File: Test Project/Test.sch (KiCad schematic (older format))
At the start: 1 part

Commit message: Summer
Added very important component layout
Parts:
- added L? (x2): 20, symbol INDUCTOR
- added R? (x2): 120, symbol R
- added U?: MCP2551-I/SN, SO-8, symbol MCP2551-I/SN
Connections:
- net at U?.6 (CANL): now also R?.2
- net at U?.7 (CANH): now also L?.2
- new net: L?.1, R?.1
- new net: L?.2, U?.7 (CANH)
- new net: R?.1, U?.6 (CANL)
- new net: L?.1, R?.2
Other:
- moved on the sheet: U?
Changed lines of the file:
@@
 LIBS:memory
 LIBS:xilinx
-LIBS:special
 LIBS:microcontrollers
 LIBS:dsp
@@
 L MCP2551-I/SN U?
 U 1 1 559C6BBA
-P 4800 3800
-F 0 "U?" H 4400 4150 50  0000 L CNN
-F 1 "MCP2551-I/SN" H 4900 4150 50  0000 L CNN
-F 2 "SO-8" H 4800 3800 50  0000 C CIN
-F 3 "" H 4800 3800 60  0000 C CNN
-	1    4800 3800
+P 4600 3600
+F 0 "U?" H 4200 3950 50  0000 L CNN
+F 1 "MCP2551-I/SN" H 4700 3950 50  0000 L CNN
+F 2 "SO-8" H 4600 3600 50  0000 C CIN
+F 3 "" H 4600 3600 60  0000 C CNN
+	1    4600 3600
 	1    0    0    -1
 $EndComp
+$Comp
+L INDUCTOR L?
+U 1 1 559DCECC
+P 6100 2400
+F 0 "L?" V 6050 2400 50  0000 C CNN
+F 1 "20" V 6200 2400 50  0000 C CNN
+F 2 "" H 6100 2400 60  0000 C CNN
+F 3 "" H 6100 2400 60  0000 C CNN
+	1    6100 2400
+	1    0    0    -1
+$EndComp
+$Comp
+L MCP2551-I/SN U?
+U 1 1 559DD087
+P 6850 3600
+F 0 "U?" H 6450 3950 50  0000 L CNN
+F 1 "MCP2551-I/SN" H 6950 3950 50  0000 L CNN
+F 2 "SO-8" H 6850 3600 50  0000 C CIN
+F 3 "" H 6850 3600 60  0000 C CNN
+	1    6850 3600
+	-1   0    0    -1
+$EndComp
+$Comp
+L INDUCTOR L?
+U 1 1 559DD128
+P 5400 2400
+F 0 "L?" V 5350 2400 50  0000 C CNN
+F 1 "20" V 5500 2400 50  0000 C CNN
+F 2 "" H 5400 2400 60  0000 C CNN
+F 3 "" H 5400 2400 60  0000 C CNN
+	1    5400 2400
+	-1   0    0    -1
+$EndComp
+Wire Wire Line
+	5400 2700 5400 3500
+Wire Wire Line
+	5400 3500 5100 3500
+$Comp
+L R R?
+U 1 1 559DD2E2
+P 5750 1600
+F 0 "R?" V 5830 1600 50  0000 C CNN
+F 1 "120" V 5750 1600 50  0000 C CNN
+F 2 "" V 5680 1600 30  0000 C CNN
+F 3 "" H 5750 1600 30  0000 C CNN
+	1    5750 1600
+	0    1    1    0
+$EndComp
+$Comp
+L R R?
+U 1 1 559DD3B4
+P 5750 3700
+F 0 "R?" V 5830 3700 50  0000 C CNN
+F 1 "120" V 5750 3700 50  0000 C CNN
+F 2 "" V 5680 3700 30  0000 C CNN
+F 3 "" H 5750 3700 30  0000 C CNN
+	1    5750 3700
+	0    1    1    0
+$EndComp
+Wire Wire Line
+	5400 1600 5600 1600
+Wire Wire Line
+	5900 1600 6100 1600
+Wire Wire Line
+	5400 2100 5400 1600
+Wire Wire Line
+	6100 1600 6100 2100
+Wire Wire Line
+	6100 2700 6100 3500
+Wire Wire Line
+	6100 3500 6350 3500
+Wire Wire Line
+	5900 3700 6350 3700
+Wire Wire Line
+	5600 3700 5100 3700
 $EndSCHEMATC

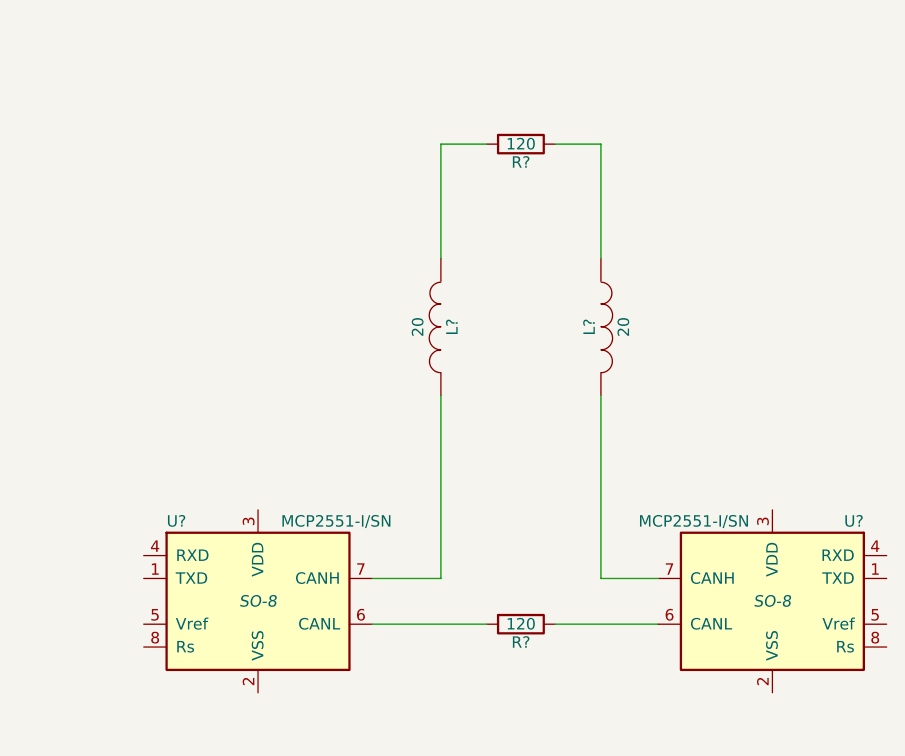
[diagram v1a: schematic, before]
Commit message: reorientation
Fixed CAN layout :(
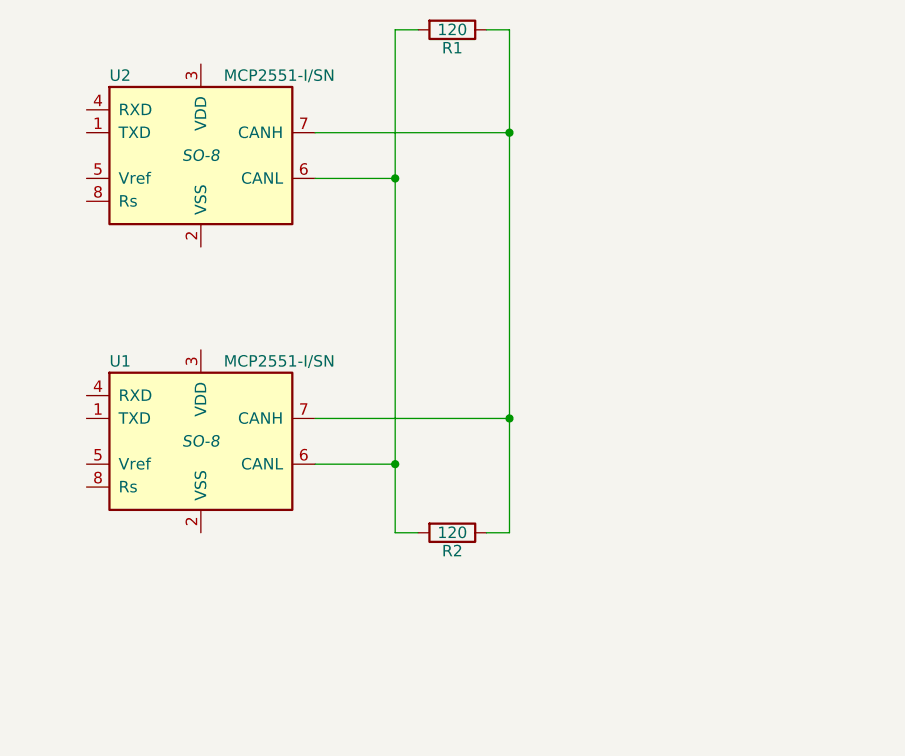
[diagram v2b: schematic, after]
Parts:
- removed L? (x2): 20, symbol INDUCTOR
- gave numbers to parts that had none: 4
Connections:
- net at R2.2, U1.6 (CANL): now also R1.2, U2.6 (CANL)
- net at U1.7 (CANH): now also R1.1, R2.1, U2.7 (CANH)
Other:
- moved on the sheet: R1, R2, U1, U2
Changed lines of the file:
@@
 LIBS:contrib
 LIBS:valves
+LIBS:Test-cache
 EELAYER 25 0
 EELAYER END
@@
 $EndDescr
 $Comp
-L MCP2551-I/SN U?
+L MCP2551-I/SN U1
 U 1 1 559C6BBA
-P 4600 3600
-F 0 "U?" H 4200 3950 50  0000 L CNN
-F 1 "MCP2551-I/SN" H 4700 3950 50  0000 L CNN
-F 2 "SO-8" H 4600 3600 50  0000 C CIN
-F 3 "" H 4600 3600 60  0000 C CNN
-	1    4600 3600
+P 4350 2900
+F 0 "U1" H 3950 3250 50  0000 L CNN
+F 1 "MCP2551-I/SN" H 4450 3250 50  0000 L CNN
+F 2 "SO-8" H 4350 2900 50  0000 C CIN
+F 3 "" H 4350 2900 60  0000 C CNN
+	1    4350 2900
 	1    0    0    -1
 $EndComp
 $Comp
-L INDUCTOR L?
-U 1 1 559DCECC
-P 6100 2400
-F 0 "L?" V 6050 2400 50  0000 C CNN
-F 1 "20" V 6200 2400 50  0000 C CNN
-F 2 "" H 6100 2400 60  0000 C CNN
-F 3 "" H 6100 2400 60  0000 C CNN
-	1    6100 2400
+L MCP2551-I/SN U2
+U 1 1 559DD087
+P 4350 1650
+F 0 "U2" H 3950 2000 50  0000 L CNN
+F 1 "MCP2551-I/SN" H 4450 2000 50  0000 L CNN
+F 2 "SO-8" H 4350 1650 50  0000 C CIN
+F 3 "" H 4350 1650 60  0000 C CNN
+	1    4350 1650
 	1    0    0    -1
 $EndComp
 $Comp
-L MCP2551-I/SN U?
-U 1 1 559DD087
-P 6850 3600
-F 0 "U?" H 6450 3950 50  0000 L CNN
-F 1 "MCP2551-I/SN" H 6950 3950 50  0000 L CNN
-F 2 "SO-8" H 6850 3600 50  0000 C CIN
-F 3 "" H 6850 3600 60  0000 C CNN
-	1    6850 3600
-	-1   0    0    -1
-$EndComp
-$Comp
-L INDUCTOR L?
-U 1 1 559DD128
-P 5400 2400
-F 0 "L?" V 5350 2400 50  0000 C CNN
-F 1 "20" V 5500 2400 50  0000 C CNN
-F 2 "" H 5400 2400 60  0000 C CNN
-F 3 "" H 5400 2400 60  0000 C CNN
-	1    5400 2400
-	-1   0    0    -1
-$EndComp
-Wire Wire Line
-	5400 2700 5400 3500
-Wire Wire Line
-	5400 3500 5100 3500
-$Comp
-L R R?
+L R R1
 U 1 1 559DD2E2
-P 5750 1600
-F 0 "R?" V 5830 1600 50  0000 C CNN
-F 1 "120" V 5750 1600 50  0000 C CNN
-F 2 "" V 5680 1600 30  0000 C CNN
-F 3 "" H 5750 1600 30  0000 C CNN
-	1    5750 1600
+P 5450 1100
+F 0 "R1" V 5530 1100 50  0000 C CNN
+F 1 "120" V 5450 1100 50  0000 C CNN
+F 2 "" V 5380 1100 30  0000 C CNN
+F 3 "" H 5450 1100 30  0000 C CNN
+	1    5450 1100
 	0    1    1    0
 $EndComp
 $Comp
-L R R?
+L R R2
 U 1 1 559DD3B4
-P 5750 3700
-F 0 "R?" V 5830 3700 50  0000 C CNN
-F 1 "120" V 5750 3700 50  0000 C CNN
-F 2 "" V 5680 3700 30  0000 C CNN
-F 3 "" H 5750 3700 30  0000 C CNN
-	1    5750 3700
+P 5450 3300
+F 0 "R2" V 5530 3300 50  0000 C CNN
+F 1 "120" V 5450 3300 50  0000 C CNN
+F 2 "" V 5380 3300 30  0000 C CNN
+F 3 "" H 5450 3300 30  0000 C CNN
+	1    5450 3300
 	0    1    1    0
 $EndComp
 Wire Wire Line
-	5400 1600 5600 1600
+	5300 1100 5200 1100
 Wire Wire Line
-	5900 1600 6100 1600
+	5200 1100 5200 3300
 Wire Wire Line
-	5400 2100 5400 1600
+	5200 3300 5300 3300
 Wire Wire Line
-	6100 1600 6100 2100
+	5600 3300 5700 3300
 Wire Wire Line
-	6100 2700 6100 3500
+	5700 3300 5700 1100
 Wire Wire Line
-	6100 3500 6350 3500
+	5700 1100 5600 1100
 Wire Wire Line
-	5900 3700 6350 3700
+	4850 1550 5700 1550
+Connection ~ 5700 1550
 Wire Wire Line
-	5600 3700 5100 3700
+	4850 1750 5200 1750
+Connection ~ 5200 1750
+Wire Wire Line
+	4850 2800 5700 2800
+Connection ~ 5700 2800
+Wire Wire Line
+	4850 3000 5200 3000
+Connection ~ 5200 3000
 $EndSCHEMATC

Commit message: test conflict commit
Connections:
- net at U1.1 (TXD): now also U2.4 (RXD)
- net at U1.4 (RXD): now also U2.1 (TXD)
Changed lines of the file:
@@
 	4850 3000 5200 3000
 Connection ~ 5200 3000
+Wire Wire Line
+	3850 1450 3550 1450
+Wire Wire Line
+	3550 1450 3550 2800
+Wire Wire Line
+	3550 2800 3850 2800
+Wire Wire Line
+	3850 2700 3650 2700
+Wire Wire Line
+	3650 2700 3650 1550
+Wire Wire Line
+	3650 1550 3850 1550
 $EndSCHEMATC
